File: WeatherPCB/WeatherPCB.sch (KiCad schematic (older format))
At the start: 1 part

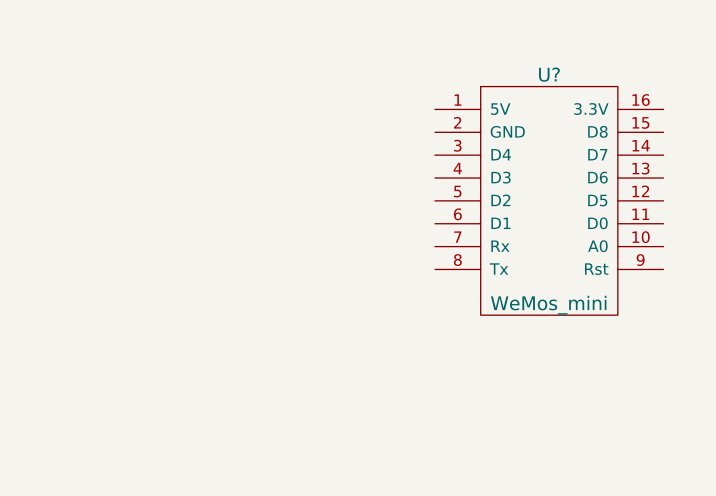
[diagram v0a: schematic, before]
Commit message: Added display and wiring
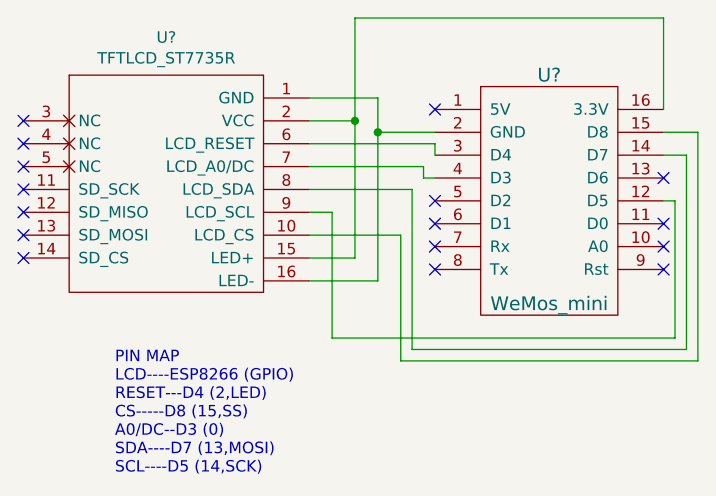
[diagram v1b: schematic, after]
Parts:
- added U?: TFTLCD_ST7735R, symbol WeatherPCB_Components:TFTLCD_ST7735R
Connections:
- net at U?.12 (D5): now also U?.9 (LCD_SCL)
- net at U?.14 (D7): now also U?.8 (LCD_SDA)
- net at U?.15 (D8): now also U?.10 (LCD_CS)
- net at U?.16 (3.3V): now also U?.15 (LED+), U?.2 (VCC)
- net at U?.2 (GND): now also U?.1 (GND), U?.16 (LED-)
- net at U?.3 (D4): now also U?.6 (LCD_RESET)
- net at U?.4 (D3): now also U?.7 (LCD_A0/DC)
- no-connect marks 0 -> 16
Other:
- note added: "PIN MAP\nLCD----ESP8266 (GPIO)\nRESET---D4 (2,LED)\nCS-----D8 (15,SS)\nA0/DC--D3 (0)\nSDA----D7 (13,MOSI)\nSCL----D5 (14,SCK)"
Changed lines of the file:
@@
 encoding utf-8
 Sheet 1 1
-Title ""
+Title "Weather Station PCB"
 Date ""
-Rev ""
-Comp ""
+Rev "1.0"
+Comp "github.com/mwyoung"
 Comment1 ""
 Comment2 ""
@@
 	1    0    0    -1
 $EndComp
+$Comp
+L WeatherPCB_Components:TFTLCD_ST7735R U?
+U 1 1 5D6562B8
+P 1550 3400
+F 0 "U?" H 1525 3965 50  0000 C CNN
+F 1 "TFTLCD_ST7735R" H 1525 3874 50  0000 C CNN
+F 2 "" H 1950 3800 50  0001 C CNN
+F 3 "" H 1950 3800 50  0001 C CNN
+F 4 "https://www.amazon.com/HiLetgo-ST7735R-128160-Display-Arduino/dp/B00LSG51MM" H 1900 4250 50  0001 C CNN "Where to Buy"
+	1    1550 3400
+	1    0    0    -1
+$EndComp
+NoConn ~ 900  3200
+NoConn ~ 900  3300
+NoConn ~ 900  3400
+NoConn ~ 900  3500
+NoConn ~ 900  3600
+NoConn ~ 900  3700
+NoConn ~ 900  3800
+Wire Wire Line
+	3700 3150 3700 2750
+Wire Wire Line
+	3700 2750 2350 2750
+Wire Wire Line
+	2350 2750 2350 3200
+Wire Wire Line
+	2350 3200 2150 3200
+Wire Wire Line
+	2350 3200 2350 3800
+Wire Wire Line
+	2350 3800 2150 3800
+Connection ~ 2350 3200
+Wire Wire Line
+	2700 3250 2450 3250
+Wire Wire Line
+	2450 3250 2450 3100
+Wire Wire Line
+	2450 3100 2150 3100
+Wire Wire Line
+	2150 3900 2450 3900
+Wire Wire Line
+	2450 3900 2450 3250
+Connection ~ 2450 3250
+Wire Wire Line
+	2150 3700 2550 3700
+Wire Wire Line
+	2550 3700 2550 4250
+Wire Wire Line
+	2550 4250 3850 4250
+Wire Wire Line
+	3850 4250 3850 3250
+Wire Wire Line
+	3850 3250 3700 3250
+Wire Wire Line
+	2150 3500 2600 3500
+Wire Wire Line
+	2600 3500 2600 4200
+Wire Wire Line
+	2600 4200 3800 4200
+Wire Wire Line
+	3800 4200 3800 3350
+Wire Wire Line
+	3800 3350 3700 3350
+Wire Wire Line
+	3750 4150 2250 4150
+Wire Wire Line
+	2250 4150 2250 3600
+Wire Wire Line
+	2250 3600 2150 3600
+Wire Wire Line
+	2150 3300 2700 3300
+Wire Wire Line
+	2700 3300 2700 3350
+Wire Wire Line
+	2150 3400 2650 3400
+Wire Wire Line
+	2650 3400 2650 3450
+Wire Wire Line
+	2650 3450 2700 3450
+NoConn ~ 3700 3450
+NoConn ~ 3700 3750
+NoConn ~ 3700 3850
+NoConn ~ 2700 3750
+NoConn ~ 2700 3650
+NoConn ~ 2700 3550
+NoConn ~ 2700 3150
+NoConn ~ 2700 3850
+Text Notes 1300 4750 0    50   ~ 0
+PIN MAP\nLCD----ESP8266 (GPIO)\nRESET---D4 (2,LED)\nCS-----D8 (15,SS)\nA0/DC--D3 (0)\nSDA----D7 (13,MOSI)\nSCL----D5 (14,SCK)
+Wire Wire Line
+	3750 3550 3700 3550
+Wire Wire Line
+	3750 3550 3750 4150
+NoConn ~ 3700 3650
 $EndSCHEMATC
